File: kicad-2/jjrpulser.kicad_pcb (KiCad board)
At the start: 2 copper layers, 20 parts, among them J1 USB_OTG, J3 Screw_Terminal_HOT, J4 Screw_Terminal_COLD, J5 Conn_UART, U1 ESP-12, U2 NCP1117-3.3_SOT223

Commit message: Разводка в процессе
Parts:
- C1, C2: footprint Capacitors_SMD:C_0805_HandSoldering -> Capacitors_Tantalum_SMD:CP_Tantalum_Case-A_EIA-3216-18_Reflow
- moved U2 17.4 mm to (155.5, 124.5), turned to 270 degrees
- moved J1 15.3 mm to (175.5, 130.8), turned to 90 degrees
- moved C1 9.66 mm to (161.0, 120.5), turned to 90 degrees
- moved R6 7.65 mm to (166.5, 118.0), turned to 90 degrees
- moved C2 3.81 mm to (148.5, 122.0), turned to 0 degrees
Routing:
- net Net-(C1-Pad1): track 71.1 -> 0.00 mm
- net Earth: track 135.0 -> 77.5 mm
- net +3V3: track 34.3 -> 46.4 mm
- net Net-(R6-Pad2): track 4.19 -> 3.15 mm

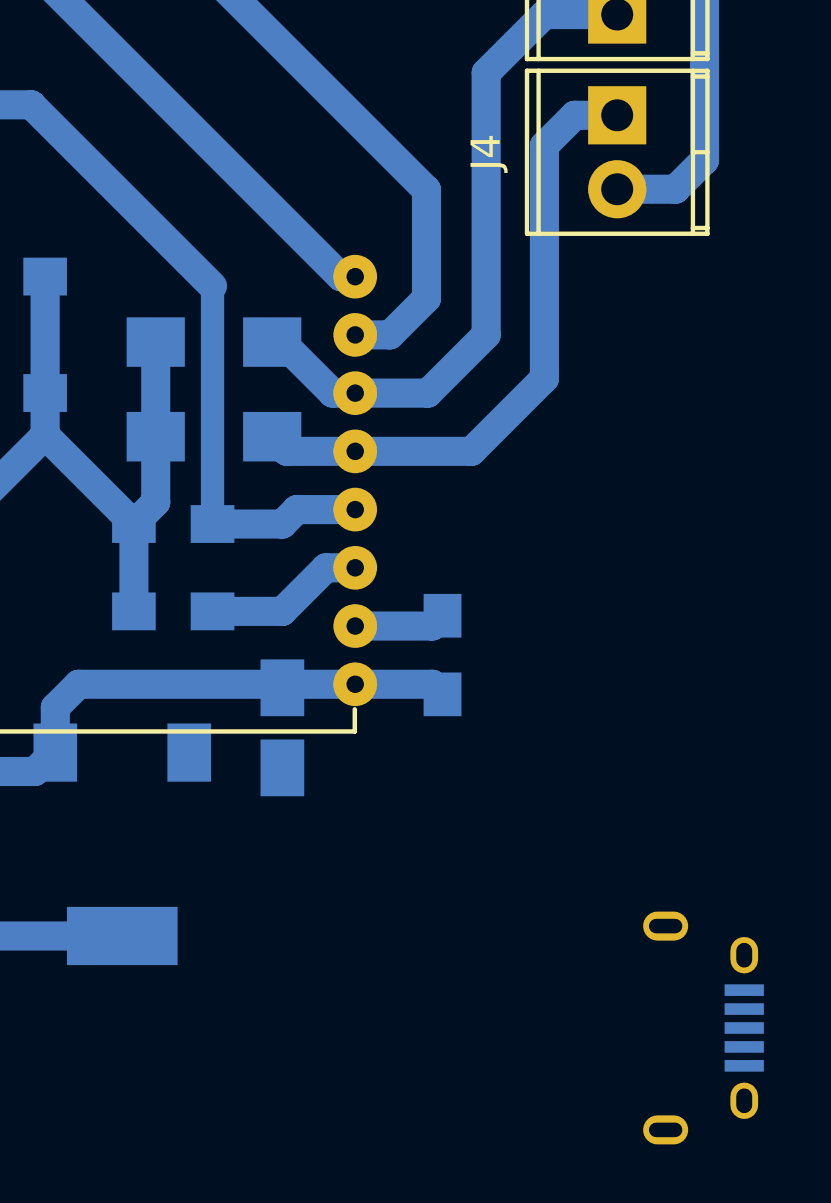
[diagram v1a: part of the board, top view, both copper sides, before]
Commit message: Новая разводка: замена micro-USB на обычный разъем питания
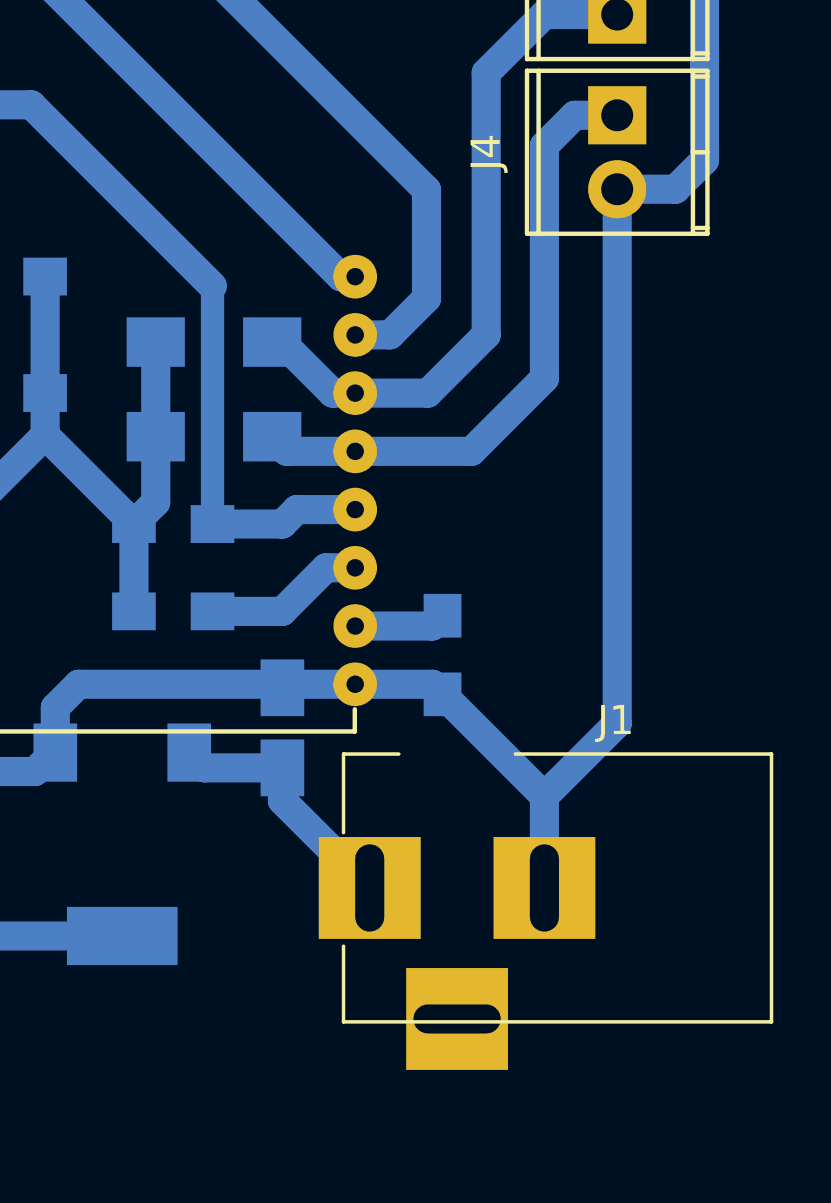
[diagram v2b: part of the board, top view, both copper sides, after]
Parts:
- C1: value 100mkF -> 10mkF 16v
- C2: value 470mkF -> 22mkF 5v
- J1: value USB_OTG -> Conn_Coaxial_Power; footprint Connectors:USB_Micro-B -> Connectors:BARREL_JACK; moved to F.Cu
- U2: value NCP1117-3.3_SOT223 -> AMS1117-3.3_SOT223
- moved J1 12.5 mm to (164.0, 126.0), turned to 180 degrees
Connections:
- net Net-(C1-Pad1) renamed +5V
- J1 pad 2: Net-(J1-Pad2) -> Earth
- J1 pad 3: Net-(J1-Pad3) -> (no net)
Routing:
- net Earth: track 77.5 -> 107.5 mm
- net +5V: track 0.00 -> 8.79 mm
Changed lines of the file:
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@@
 (kicad_pcb (version 4) (host pcbnew 4.0.7)
   (general
-    (links 41)
-    (no_connects 7)
-    (area 138.003333 82.824999 179.729 135.535001)
+    (links 38)
+    (no_connects 0)
+    (area 138.003333 82.824999 178.125001 132.980952)
     (thickness 1.6)
     (drawings 0)
-    (tracks 87)
+    (tracks 95)
     (zones 0)
     (modules 20)
-    (nets 22)
+    (nets 18)
   )
   (page A4)
@@
   (net 15 "Net-(J4-Pad1)")
   (net 16 "Net-(J3-Pad2)")
-  (net 17 "Net-(C1-Pad1)")
-  (net 18 "Net-(J1-Pad2)")
-  (net 19 "Net-(J1-Pad3)")
-  (net 20 "Net-(J1-Pad4)")
-  (net 21 "Net-(J1-Pad6)")
+  (net 17 +5V)
   (net_class Default "Это класс цепей по умолчанию."
     (clearance 0.1)
@@
     (uvia_dia 0.3)
     (uvia_drill 0.1)
-    (add_net "Net-(C1-Pad1)")
+    (add_net +5V)
     (add_net "Net-(D1-Pad2)")
     (add_net "Net-(D2-Pad2)")
-    (add_net "Net-(J1-Pad2)")
-    (add_net "Net-(J1-Pad3)")
-    (add_net "Net-(J1-Pad4)")
-    (add_net "Net-(J1-Pad6)")
     (add_net "Net-(J3-Pad2)")
     (add_net "Net-(J4-Pad1)")
@@
     (add_net Earth)
   )
+  (module Connectors:BARREL_JACK (layer F.Cu)
+    (at 164 126 180)
+    (descr "DC Barrel Jack")
+    (tags "Power Jack")
+    (fp_text reference J1 (at -8.45 5.75 360) (layer F.SilkS)
+      (effects (font (size 1 1) (thickness 0.15)))
+    )
+    (fp_text value Conn_Coaxial_Power (at -6.2 -5.5 180) (layer F.Fab)
+      (effects (font (size 1 1) (thickness 0.15)))
+    )
+    (fp_line (start 1 -4.5) (end 1 -4.75) (layer F.CrtYd) (width 0.05))
+    (fp_line (start 1 -4.75) (end -14 -4.75) (layer F.CrtYd) (width 0.05))
+    (fp_line (start 1 -4.5) (end 1 -2) (layer F.CrtYd) (width 0.05))
+    (fp_line (start 1 -2) (end 2 -2) (layer F.CrtYd) (width 0.05))
+    (fp_line (start 2 -2) (end 2 2) (layer F.CrtYd) (width 0.05))
+    (fp_line (start 2 2) (end 1 2) (layer F.CrtYd) (width 0.05))
+    (fp_line (start 1 2) (end 1 4.75) (layer F.CrtYd) (width 0.05))
+    (fp_line (start 1 4.75) (end -1 4.75) (layer F.CrtYd) (width 0.05))
+    (fp_line (start -1 4.75) (end -5 4.75) (layer F.CrtYd) (width 0.05))
+    (fp_line (start -5 4.75) (end -14 4.75) (layer F.CrtYd) (width 0.05))
+    (fp_line (start -14 4.75) (end -14 -4.75) (layer F.CrtYd) (width 0.05))
+    (fp_line (start -5 4.6) (end -13.8 4.6) (layer F.SilkS) (width 0.12))
+    (fp_line (start -13.8 4.6) (end -13.8 -4.6) (layer F.SilkS) (width 0.12))
+    (fp_line (start 0.9 1.9) (end 0.9 4.6) (layer F.SilkS) (width 0.12))
+    (fp_line (start 0.9 4.6) (end -1 4.6) (layer F.SilkS) (width 0.12))
+    (fp_line (start -13.8 -4.6) (end 0.9 -4.6) (layer F.SilkS) (width 0.12))
+    (fp_line (start 0.9 -4.6) (end 0.9 -2) (layer F.SilkS) (width 0.12))
+    (fp_line (start -10.2 -4.5) (end -10.2 4.5) (layer F.Fab) (width 0.1))
+    (fp_line (start -13.7 -4.5) (end -13.7 4.5) (layer F.Fab) (width 0.1))
+    (fp_line (start -13.7 4.5) (end 0.8 4.5) (layer F.Fab) (width 0.1))
+    (fp_line (start 0.8 4.5) (end 0.8 -4.5) (layer F.Fab) (width 0.1))
+    (fp_line (start 0.8 -4.5) (end -13.7 -4.5) (layer F.Fab) (width 0.1))
+    (pad 1 thru_hole rect (at 0 0 180) (size 3.5 3.5) (drill oval 1 3) (layers *.Cu *.Mask)
+      (net 17 +5V))
+    (pad 2 thru_hole rect (at -6 0 180) (size 3.5 3.5) (drill oval 1 3) (layers *.Cu *.Mask)
+      (net 1 Earth))
+    (pad 3 thru_hole rect (at -3 -4.5 180) (size 3.5 3.5) (drill oval 3 1) (layers *.Cu *.Mask))
+  )
   (module TO_SOT_Packages_SMD:SOT-223-3Lead_TabPin2 (layer B.Cu)
     (at 155.5 124.5 270)
@@
       (effects (font (size 1 1) (thickness 0.15)) (justify mirror))
     )
-    (fp_text value NCP1117-3.3_SOT223 (at 0 -4.5 270) (layer B.Fab)
+    (fp_text value AMS1117-3.3_SOT223 (at 0 -4.5 270) (layer B.Fab)
       (effects (font (size 1 1) (thickness 0.15)) (justify mirror))
     )
@@
       (net 4 +3V3))
     (pad 3 smd rect (at -3.15 -2.3 270) (size 2 1.5) (layers B.Cu B.Paste B.Mask)
-      (net 17 "Net-(C1-Pad1)"))
+      (net 17 +5V))
     (pad 1 smd rect (at -3.15 2.3 270) (size 2 1.5) (layers B.Cu B.Paste B.Mask)
       (net 1 Earth))
@@
     )
   )
-  (module Connectors:USB_Micro-B (layer B.Cu)
-    (at 175.514 130.81 90)
-    (descr "Micro USB Type B Receptacle")
-    (tags "USB USB_B USB_micro USB_OTG")
-    (attr smd)
-    (fp_text reference J1 (at 0 3.24 90) (layer B.SilkS)
-      (effects (font (size 1 1) (thickness 0.15)) (justify mirror))
-    )
-    (fp_text value USB_OTG (at 0 -5.01 90) (layer B.Fab)
-      (effects (font (size 1 1) (thickness 0.15)) (justify mirror))
-    )
-    (fp_line (start -4.6 2.59) (end 4.6 2.59) (layer B.CrtYd) (width 0.05))
-    (fp_line (start 4.6 2.59) (end 4.6 -4.26) (layer B.CrtYd) (width 0.05))
-    (fp_line (start 4.6 -4.26) (end -4.6 -4.26) (layer B.CrtYd) (width 0.05))
-    (fp_line (start -4.6 -4.26) (end -4.6 2.59) (layer B.CrtYd) (width 0.05))
-    (fp_line (start -4.35 -4.03) (end 4.35 -4.03) (layer B.SilkS) (width 0.12))
-    (fp_line (start -4.35 2.38) (end 4.35 2.38) (layer B.SilkS) (width 0.12))
-    (fp_line (start 4.35 2.38) (end 4.35 -4.03) (layer B.SilkS) (width 0.12))
-    (fp_line (start 4.35 -2.8) (end -4.35 -2.8) (layer B.SilkS) (width 0.12))
-    (fp_line (start -4.35 -4.03) (end -4.35 2.38) (layer B.SilkS) (width 0.12))
-    (pad 1 smd rect (at -1.3 1.35) (size 1.35 0.4) (layers B.Cu B.Paste B.Mask)
-      (net 17 "Net-(C1-Pad1)"))
-    (pad 2 smd rect (at -0.65 1.35) (size 1.35 0.4) (layers B.Cu B.Paste B.Mask)
-      (net 18 "Net-(J1-Pad2)"))
-    (pad 3 smd rect (at 0 1.35) (size 1.35 0.4) (layers B.Cu B.Paste B.Mask)
-      (net 19 "Net-(J1-Pad3)"))
-    (pad 4 smd rect (at 0.65 1.35) (size 1.35 0.4) (layers B.Cu B.Paste B.Mask)
-      (net 20 "Net-(J1-Pad4)"))
-    (pad 5 smd rect (at 1.3 1.35) (size 1.35 0.4) (layers B.Cu B.Paste B.Mask)
-      (net 1 Earth))
-    (pad 6 thru_hole oval (at -2.5 1.35) (size 0.95 1.25) (drill oval 0.55 0.85) (layers *.Cu *.Mask)
-      (net 21 "Net-(J1-Pad6)"))
-    (pad 6 thru_hole oval (at 2.5 1.35) (size 0.95 1.25) (drill oval 0.55 0.85) (layers *.Cu *.Mask)
-      (net 21 "Net-(J1-Pad6)"))
-    (pad 6 thru_hole oval (at -3.5 -1.35) (size 1.55 1) (drill oval 1.15 0.5) (layers *.Cu *.Mask)
-      (net 21 "Net-(J1-Pad6)"))
-    (pad 6 thru_hole oval (at 3.5 -1.35) (size 1.55 1) (drill oval 1.15 0.5) (layers *.Cu *.Mask)
-      (net 21 "Net-(J1-Pad6)"))
-  )
   (module Capacitors_Tantalum_SMD:CP_Tantalum_Case-A_EIA-3216-18_Reflow (layer B.Cu)
     (at 148.5 122)
@@
       (effects (font (size 1 1) (thickness 0.15)) (justify mirror))
     )
-    (fp_text value 470mkF (at 0 -2.55) (layer B.Fab)
+    (fp_text value "22mkF 5v" (at 0 -2.55) (layer B.Fab)
       (effects (font (size 1 1) (thickness 0.15)) (justify mirror))
     )
@@
       (effects (font (size 1 1) (thickness 0.15)) (justify mirror))
     )
-    (fp_text value 100mkF (at 0 -2.55 90) (layer B.Fab)
+    (fp_text value "10mkF 16v" (at 0 -2.55 90) (layer B.Fab)
       (effects (font (size 1 1) (thickness 0.15)) (justify mirror))
     )
@@
     (fp_line (start -2.65 1.05) (end -2.65 -1.05) (layer B.SilkS) (width 0.12))
     (pad 1 smd rect (at -1.375 0 90) (size 1.95 1.5) (layers B.Cu B.Paste B.Mask)
-      (net 17 "Net-(C1-Pad1)"))
+      (net 17 +5V))
     (pad 2 smd rect (at 1.375 0 90) (size 1.95 1.5) (layers B.Cu B.Paste B.Mask)
       (net 1 Earth))
@@
     )
   )
+  (segment (start 172.5 102) (end 172.5 120.35) (width 1) (layer B.Cu) (net 1))
+  (segment (start 172.5 120.35) (end 170 122.85) (width 1) (layer B.Cu) (net 1))
+  (segment (start 166.5 119.35) (end 170 122.85) (width 1) (layer B.Cu) (net 1))
+  (segment (start 170 122.85) (end 170 126) (width 1) (layer B.Cu) (net 1))
   (segment (start 163.5011 119.0036) (end 161.1214 119.0036) (width 1) (layer B.Cu) (net 1))
   (segment (start 161.1214 119.0036) (end 153.9964 119.0036) (width 1) (layer B.Cu) (net 1))
@@
   (segment (start 143.54 103.5) (end 143.5 103.54) (width 1) (layer B.Cu) (net 3))
   (segment (start 143.5 103.54) (end 143.5 107.15) (width 1) (layer B.Cu) (net 3))
-  (segment (start 147.5011 119.0036) (end 147.125 119.3797) (width 1) (layer B.Cu) (net 4) (status C00000))
-  (segment (start 147.125 119.3797) (end 147.125 122) (width 1) (layer B.Cu) (net 4) (status C00000))
+  (segment (start 147.5011 119.0036) (end 147.125 119.3797) (width 1) (layer B.Cu) (net 4))
+  (segment (start 147.125 119.3797) (end 147.125 122) (width 1) (layer B.Cu) (net 4))
   (segment (start 155.5 127.65) (end 149.65 127.65) (width 1) (layer B.Cu) (net 4))
   (segment (start 147.125 125.125) (end 147.125 122) (width 1) (layer B.Cu) (net 4))
@@
   (segment (start 160.975 107.25) (end 162.7286 109.0036) (width 1) (layer B.Cu) (net 16))
   (segment (start 162.7286 109.0036) (end 163.5011 109.0036) (width 1) (layer B.Cu) (net 16))
+  (segment (start 161 121.875) (end 161 123) (width 1) (layer B.Cu) (net 17))
+  (segment (start 161 123) (end 164 126) (width 1) (layer B.Cu) (net 17))
+  (segment (start 157.8 121.35) (end 158.325 121.875) (width 1) (layer B.Cu) (net 17))
+  (segment (start 158.325 121.875) (end 161 121.875) (width 1) (layer B.Cu) (net 17))
 )

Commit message: Новая разводка - WIP
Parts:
- moved D2 17.8 mm to (142.2, 121.2)
- moved D1 16.3 mm to (142.2, 109.8)
- moved R1 14.3 mm to (144.8, 112.8)
- moved J3 12.8 mm to (168.8, 108.2)
- moved J4 12.8 mm to (168.8, 114.2)
- moved R4 9.83 mm to (144.8, 118.2), turned to 90 degrees
- moved J1 3.51 mm to (160.5, 125.8)
- moved C2 1.58 mm to (150.0, 121.5)
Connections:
- J1 pad 3: (no net) -> Earth
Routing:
- net Net-(J3-Pad2): track 23.2 -> 9.14 mm
- net Net-(R1-Pad2): track 16.8 -> 3.13 mm
- net Net-(J4-Pad1): track 21.5 -> 8.60 mm
- net Net-(R4-Pad2): track 9.40 -> 2.79 mm
- net Earth: track 107.5 -> 103.2 mm
- net Net-(D2-Pad2): track 3.67 -> 1.67 mm
- net Net-(D1-Pad2): track 3.67 -> 1.67 mm
- net +5V: track 8.79 -> 7.50 mm
- net +3V3: track 46.4 -> 45.3 mm
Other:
- board outline added: 33 x 48 mm

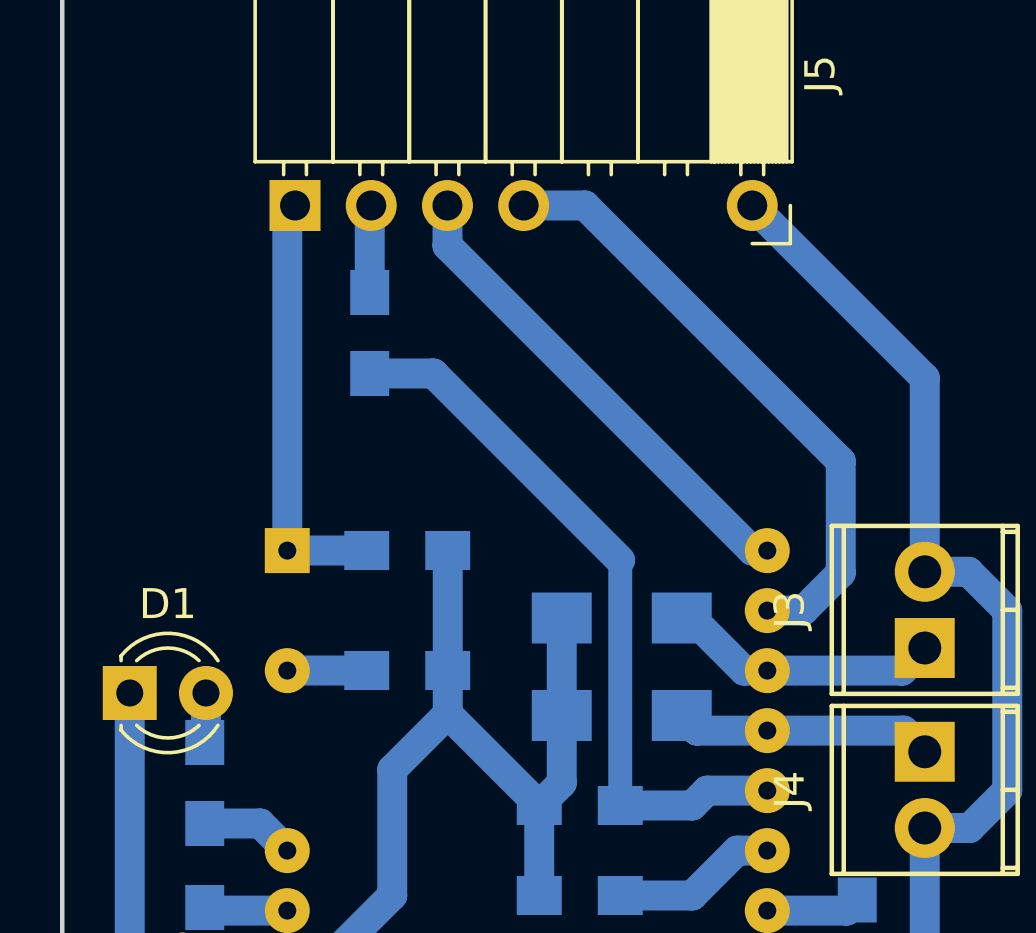
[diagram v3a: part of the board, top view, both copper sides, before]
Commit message: Разводка2: +5V с UART - программирование и консоль без внешнего питания. GPIO16 <--> RESET - выход из deep sleep
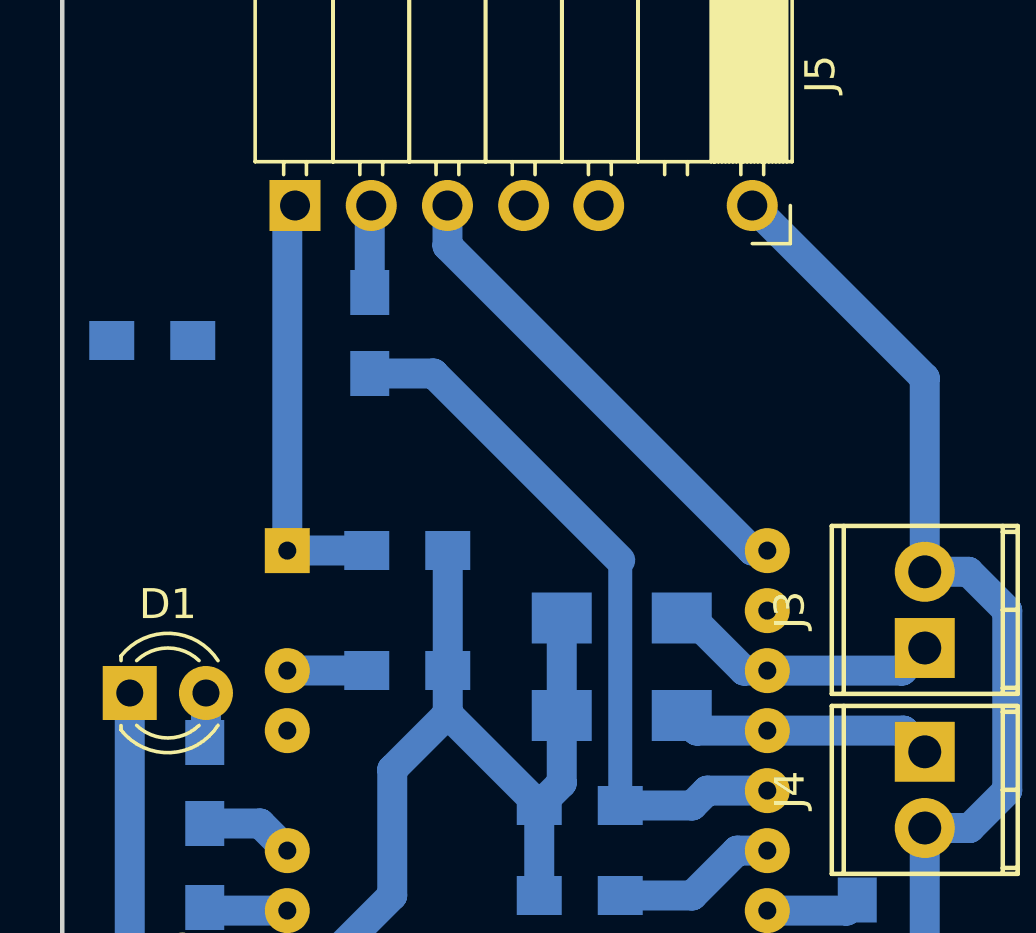
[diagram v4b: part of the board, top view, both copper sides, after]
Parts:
- added R11: 470, Resistors_SMD:R_0805_HandSoldering, B.Cu at (143.0, 98.0)
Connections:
- J1 pad 3: Earth -> (no net)
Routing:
- net Net-(J5-Pad4): track 20.8 -> 0.00 mm

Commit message: Новая разводка
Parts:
- added R12: 470, Resistors_SMD:R_0805_HandSoldering, B.Cu at (152.9, 96.5)
- added R13: 470, Resistors_SMD:R_0805_HandSoldering, B.Cu at (155.4, 96.5)
- added R14: 470, Resistors_SMD:R_0805_HandSoldering, B.Cu at (147.8, 96.5)
- moved R11 8.73 mm to (145.0, 106.5), turned to 90 degrees
- moved R1 2.02 mm to (144.5, 114.8), turned to 0 degrees
- moved D1 1.58 mm to (141.8, 111.2), turned to 315 degrees
- moved R9 1.25 mm to (150.3, 96.5)
- moved R4 1.03 mm to (144.5, 117.2), turned to 0 degrees
- moved D2 0.71 mm to (141.8, 120.8), turned to 45 degrees
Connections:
- J1 pad 3: (no net) -> Earth
- R11 pad 2: Net-(J5-Pad1) -> Net-(R11-Pad2)
- R2 pad 1: Net-(J5-Pad1) -> Net-(R11-Pad2)
- U1 pad 1: Net-(J5-Pad1) -> Net-(R11-Pad2)
- U1 pad 15: Net-(J5-Pad4) -> Net-(R13-Pad2)
- U1 pad 16: Net-(J5-Pad3) -> Net-(R12-Pad1)
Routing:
- net +5V: track 7.50 -> 40.8 mm
- net Net-(R13-Pad2): track 0.00 -> 19.1 mm
- net Net-(J5-Pad3): track 16.2 -> 1.67 mm
- net Net-(R12-Pad1): track 0.00 -> 14.2 mm
- net Net-(J5-Pad1): track 14.3 -> 1.67 mm
- net Net-(R11-Pad2): track 0.00 -> 12.5 mm
- net Net-(R11-Pad1): track 0.00 -> 4.77 mm
- net Earth: track 103.2 -> 101.2 mm
- net Net-(R8-Pad2): track 24.2 -> 26.3 mm
- net Net-(J5-Pad4): track 0.00 -> 1.66 mm
- net Net-(R1-Pad2): track 3.13 -> 1.76 mm
- net Net-(J5-Pad2): track 2.92 -> 1.65 mm
- net Net-(R4-Pad2): track 2.79 -> 1.75 mm
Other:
- board size 33 x 48 mm -> 33.8 x 48 mm
